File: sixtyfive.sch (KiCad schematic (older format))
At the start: 169 parts, among them J1 Conn_01x12, J2 Conn_ARM_JTAG_SWD_10, Q1 BSS138, SW1 SW_Push, U1 USBLC6-2SC6, U2 STM32F072C8Tx, U3 MCP1700-3302E_SOT23

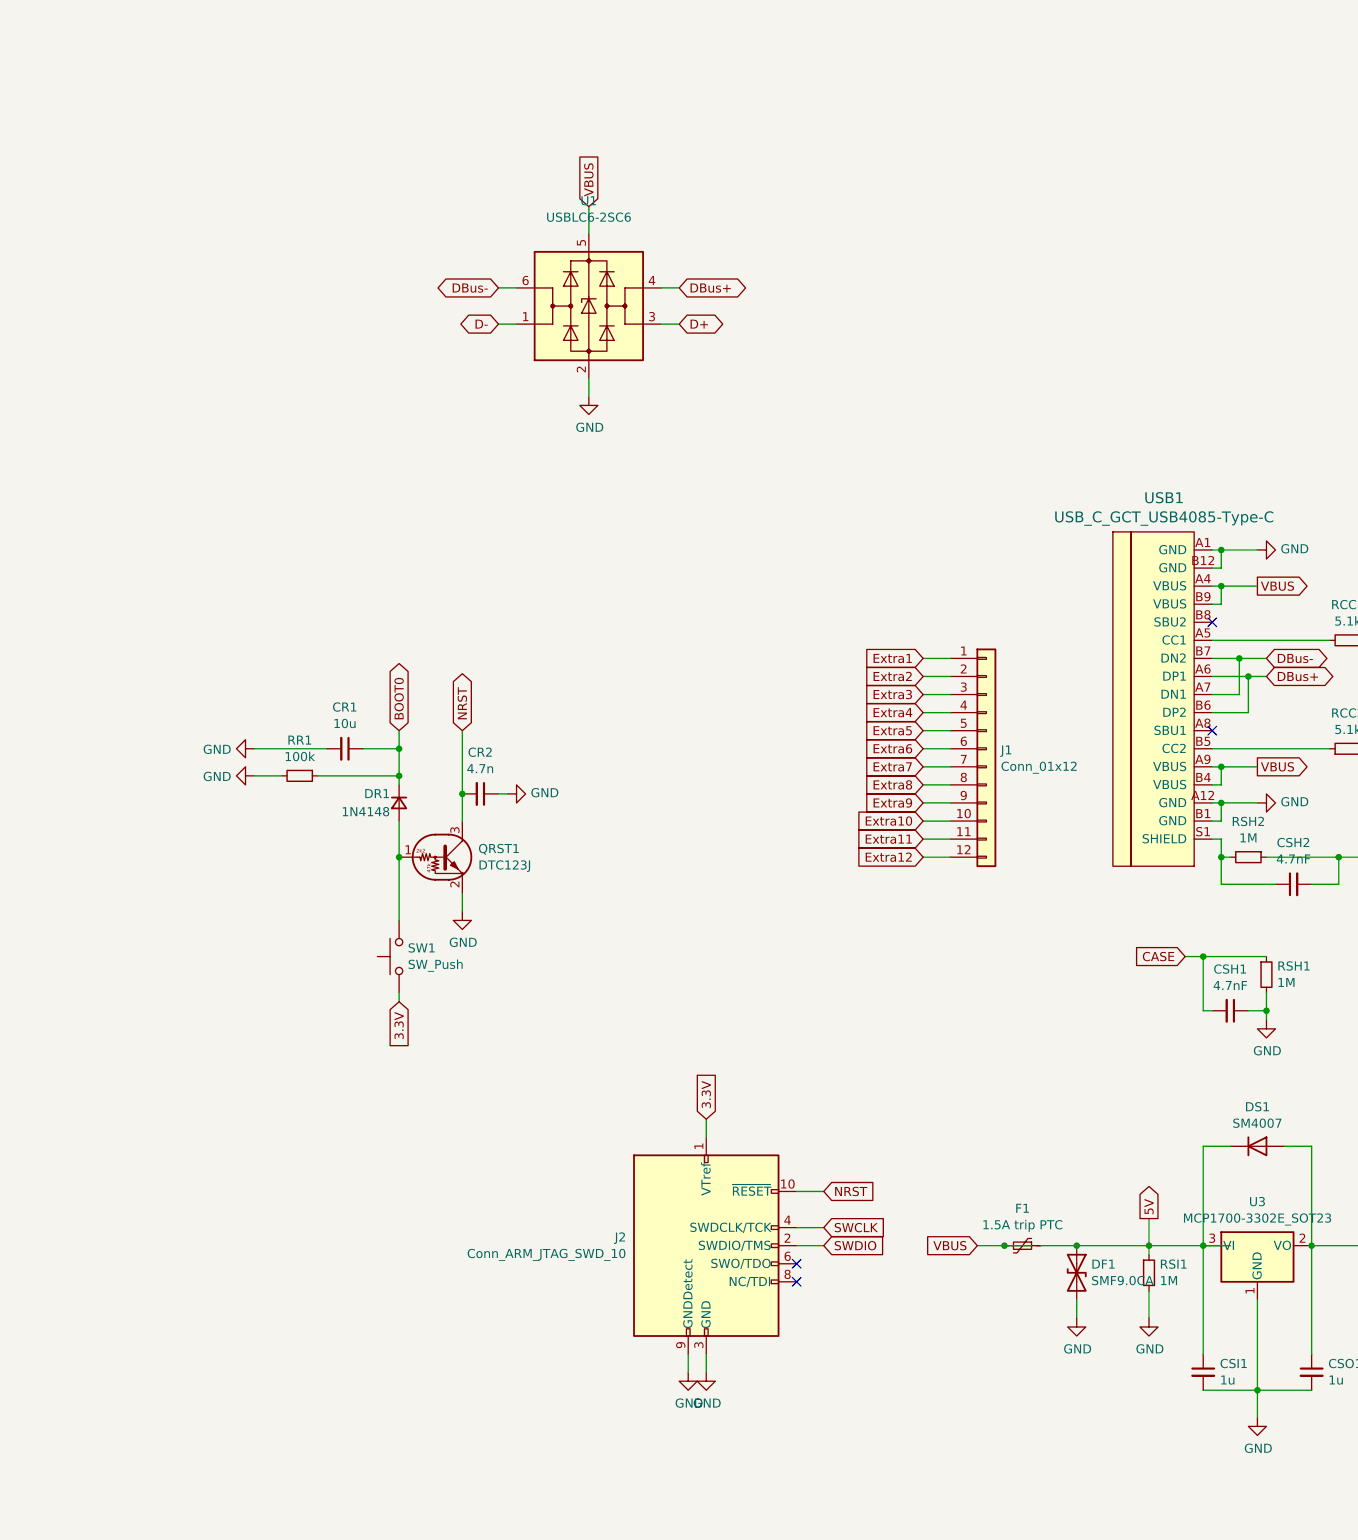
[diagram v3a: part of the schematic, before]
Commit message: swapped a couple components for basic parts, rerouted
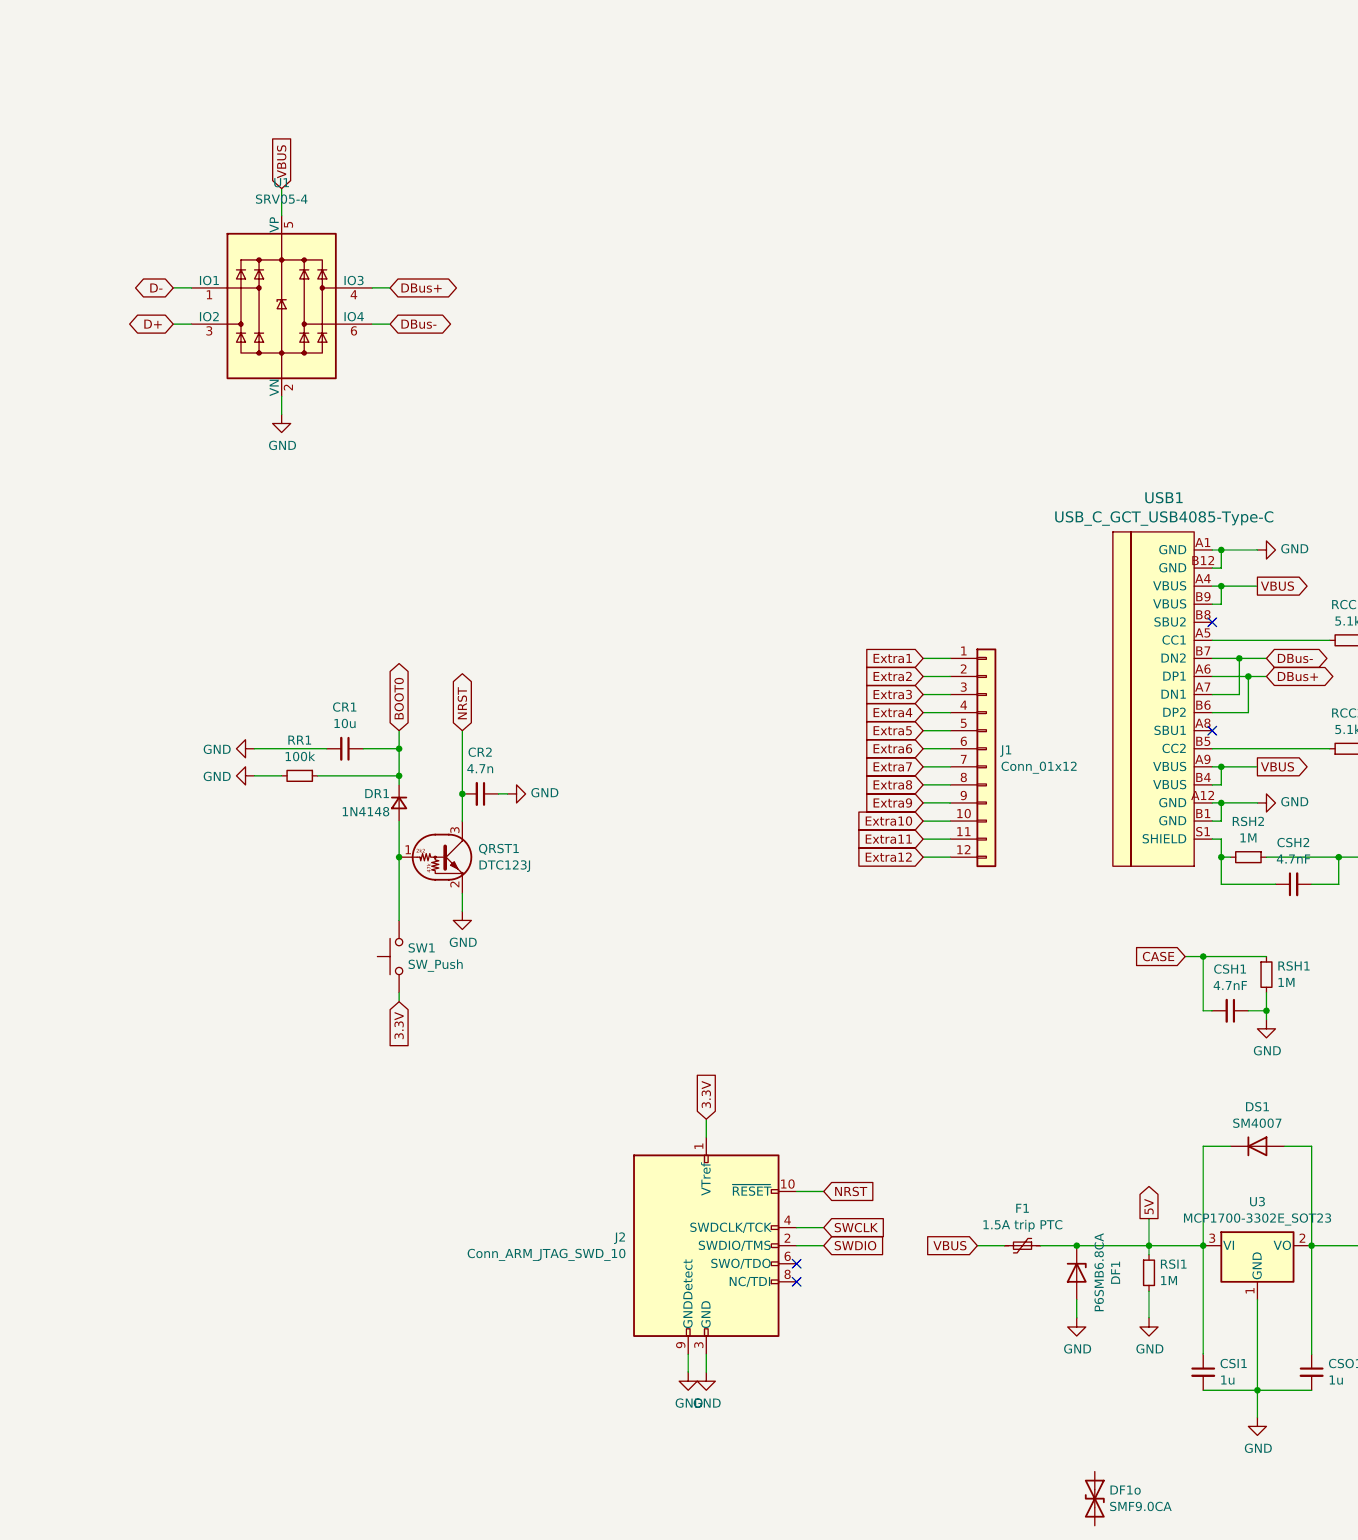
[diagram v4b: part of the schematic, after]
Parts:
- removed U1: USBLC6-2SC6, Package_TO_SOT_SMD:SOT-23-6, symbol Power_Protection:USBLC6-2SC6
- added DF1: P6SMB6.8CA, Diode_SMD:D_SMB, symbol Diode:Z2SMBxxx
- added U1: SRV05-4, Package_TO_SOT_SMD:SOT-23-6, symbol Power_Protection:SRV05-4
- renumbered DF1 to DF1o
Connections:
- net 5V: now also DF1.1 (K); no longer DF1o.1 (A1)
- net D+: now also U1.3 (IO2)
- net D-: now also U1.1 (IO1)
- net DBus+: now also U1.4 (IO3)
- net DBus-: now also U1.6 (IO4)
- net GND: now also DF1.2 (A), U1.2 (VN); no longer DF1o.2 (A2)
- net VBUS: now also U1.5 (VP)
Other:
- moved on the sheet: DF1o
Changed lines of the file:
@@
 $EndComp
 $Comp
-L Device:D_TVS DF1
+L Device:D_TVS DF1o
 U 1 1 5F1046D2
-P 24050 21000
-F 0 "DF1" V 24004 21080 50  0000 L CNN
-F 1 "SMF9.0CA" V 24095 21080 50  0000 L CNN
-F 2 "Diode_SMD:D_SOD-123" H 24050 21000 50  0001 C CNN
-F 3 "~" H 24050 21000 50  0001 C CNN
-F 4 "C123799" V 24050 21000 50  0001 C CNN "JLCCode"
-	1    24050 21000
+P 24150 22250
+F 0 "DF1o" V 24104 22330 50  0000 L CNN
+F 1 "SMF9.0CA" V 24195 22330 50  0000 L CNN
+F 2 "Diode_SMD:D_SOD-123" H 24150 22250 50  0001 C CNN
+F 3 "~" H 24150 22250 50  0001 C CNN
+F 4 "C123799" V 24150 22250 50  0001 C CNN "JLCCode"
+	1    24150 22250
 	0    1    1    0
 $EndComp
 Wire Wire Line
-	23850 20850 24050 20850
-Wire Wire Line
-	24050 20850 24450 20850
-Wire Wire Line
 	24450 20850 24450 20900
-Connection ~ 24050 20850
-$Comp
-L Regulator_Linear:MCP1700-3302E_SOT23 U3
-U 1 1 5F106F9B
-P 25050 20850
-F 0 "U3" H 25050 21092 50  0000 C CNN
-F 1 "MCP1700-3302E_SOT23" H 25050 21001 50  0000 C CNN
-F 2 "Package_TO_SOT_SMD:SOT-23" H 25050 21075 50  0001 C CNN
-F 3 "http://ww1.microchip.com/downloads/en/DeviceDoc/20001826D.pdf" H 25050 20850 50  0001 C CNN
-F 4 "C39051" H 25050 20850 50  0001 C CNN "JLCCode"
-	1    25050 20850
-	1    0    0    -1
-$EndComp
 Connection ~ 24450 20850
 $Comp
@@
 Connection ~ 24850 18400
 Wire Wire Line
-	24750 20850 24900 20850
-Wire Wire Line
 	24450 20850 24750 20850
 Wire Wire Line
@@
 	0    -1   -1   0
 $EndComp
-$Comp
-L Power_Protection:USBLC6-2SC6 U1
-U 1 1 60E168FE
-P 21350 15650
-F 0 "U1" H 21350 16231 50  0000 C CNN
-F 1 "USBLC6-2SC6" H 21350 16140 50  0000 C CNN
-F 2 "Package_TO_SOT_SMD:SOT-23-6" H 21350 15150 50  0001 C CNN
-F 3 "https://www.st.com/resource/en/datasheet/usblc6-2.pdf" H 21550 16000 50  0001 C CNN
-F 4 "C7519" H 21350 15650 50  0001 C CNN "JLCPCB"
-	1    21350 15650
-	1    0    0    -1
-$EndComp
-Text GLabel 21350 15100 1    50   Input ~ 0
+Text GLabel 19650 15000 1    50   Input ~ 0
 VBUS
 Wire Wire Line
-	21350 15100 21350 15250
+	19650 15000 19650 15150
 $Comp
 L power:GND #PWR0141
 U 1 1 60E63053
-P 21350 16150
-F 0 "#PWR0141" H 21350 15900 50  0001 C CNN
-F 1 "GND" H 21355 15977 50  0000 C CNN
-F 2 "" H 21350 16150 50  0001 C CNN
-F 3 "" H 21350 16150 50  0001 C CNN
-	1    21350 16150
+P 19650 16250
+F 0 "#PWR0141" H 19650 16000 50  0001 C CNN
+F 1 "GND" H 19655 16077 50  0000 C CNN
+F 2 "" H 19650 16250 50  0001 C CNN
+F 3 "" H 19650 16250 50  0001 C CNN
+	1    19650 16250
 	1    0    0    -1
 $EndComp
 Wire Wire Line
-	21350 16150 21350 16050
-Text GLabel 21850 15750 2    50   BiDi ~ 0
+	19650 16250 19650 16150
+Text GLabel 19050 15750 0    50   BiDi ~ 0
 D+
-Text GLabel 20850 15750 0    50   BiDi ~ 0
+Text GLabel 19050 15550 0    50   BiDi ~ 0
 D-
-Text GLabel 20850 15550 0    50   BiDi ~ 0
+Text GLabel 20250 15750 2    50   BiDi ~ 0
 DBus-
-Text GLabel 21850 15550 2    50   BiDi ~ 0
+Text GLabel 20250 15550 2    50   BiDi ~ 0
 DBus+
 Wire Wire Line
-	20950 15550 20850 15550
+	20150 15750 20250 15750
 Wire Wire Line
-	20850 15750 20950 15750
+	19050 15550 19150 15550
 Wire Wire Line
-	21750 15750 21850 15750
+	19150 15750 19050 15750
 Wire Wire Line
-	21850 15550 21750 15550
+	20250 15550 20150 15550
 $Comp
 L power:GNDD #PWR0142
@@
 Wire Wire Line
 	23650 20850 23500 20850
-Connection ~ 23650 20850
-Wire Wire Line
-	23650 20850 23800 20850
 $Comp
 L Diode:BAV70 D1
@@
 Wire Wire Line
 	25350 20850 25800 20850
+$Comp
+L Power_Protection:SRV05-4 U1
+U 1 1 5EEE073D
+P 19650 15650
+F 0 "U1" H 19650 16331 50  0000 C CNN
+F 1 "SRV05-4" H 19650 16240 50  0000 C CNN
+F 2 "Package_TO_SOT_SMD:SOT-23-6" H 20350 15200 50  0001 C CNN
+F 3 "http://www.onsemi.com/pub/Collateral/SRV05-4-D.PDF" H 19650 15650 50  0001 C CNN
+F 4 "C85364" H 19650 15650 50  0001 C CNN "JLCCode"
+	1    19650 15650
+	1    0    0    -1
+$EndComp
+$Comp
+L Regulator_Linear:MCP1700-3302E_SOT23 U3
+U 1 1 5F106F9B
+P 25050 20850
+F 0 "U3" H 25050 21092 50  0000 C CNN
+F 1 "MCP1700-3302E_SOT23" H 25050 21001 50  0000 C CNN
+F 2 "Package_TO_SOT_SMD:SOT-23" H 25050 21075 50  0001 C CNN
+F 3 "http://ww1.microchip.com/downloads/en/DeviceDoc/20001826D.pdf" H 25050 20850 50  0001 C CNN
+F 4 "C39051" H 25050 20850 50  0001 C CNN "JLCCode"
+	1    25050 20850
+	1    0    0    -1
+$EndComp
+$Comp
+L Diode:Z2SMBxxx DF1
+U 1 1 5F28F23A
+P 24050 21000
+F 0 "DF1" H 24050 21217 50  0000 C CNN
+F 1 "P6SMB6.8CA" H 24050 21126 50  0000 C CNN
+F 2 "Diode_SMD:D_SMB" H 24050 20825 50  0001 C CNN
+F 3 "https://datasheet.lcsc.com/szlcsc/Brightking-Elec-TAIWAN-P6SMB6-8CA_C78395.pdf" H 24050 21000 50  0001 C CNN
+F 4 "C78395" H 24050 21000 50  0001 C CNN "JLCCode"
+	1    24050 21000
+	0    1    1    0
+$EndComp
+Wire Wire Line
+	23850 20850 24050 20850
+Connection ~ 24050 20850
+Wire Wire Line
+	24050 20850 24450 20850
 $EndSCHEMATC

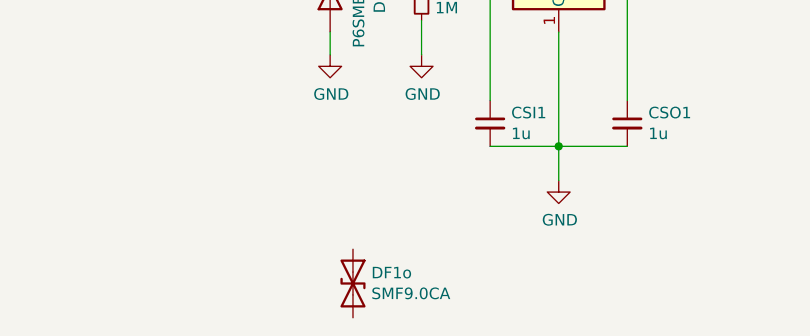
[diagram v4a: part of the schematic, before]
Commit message: Didn't quite save everything that last time.
Just following the last bit of advice from the discord, swapping a couple components and rerouting some things
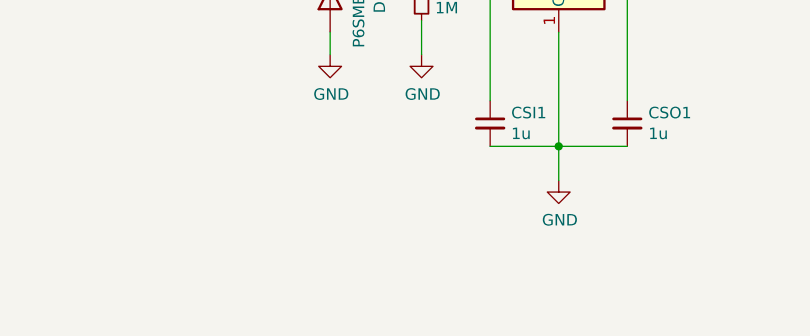
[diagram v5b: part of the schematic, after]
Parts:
- removed DF1o: SMF9.0CA, Diode_SMD:D_SOD-123, symbol Device:D_TVS
- DF1: footprint Diode_SMD:D_SMB -> Diode_SMD:D_SOD-123
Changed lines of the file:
@@
 	1    0    0    -1
 $EndComp
-$Comp
-L Device:D_TVS DF1o
-U 1 1 5F1046D2
-P 24150 22250
-F 0 "DF1o" V 24104 22330 50  0000 L CNN
-F 1 "SMF9.0CA" V 24195 22330 50  0000 L CNN
-F 2 "Diode_SMD:D_SOD-123" H 24150 22250 50  0001 C CNN
-F 3 "~" H 24150 22250 50  0001 C CNN
-F 4 "C123799" V 24150 22250 50  0001 C CNN "JLCCode"
-	1    24150 22250
-	0    1    1    0
-$EndComp
 Wire Wire Line
 	24450 20850 24450 20900
@@
 F 0 "DF1" H 24050 21217 50  0000 C CNN
 F 1 "P6SMB6.8CA" H 24050 21126 50  0000 C CNN
-F 2 "Diode_SMD:D_SMB" H 24050 20825 50  0001 C CNN
+F 2 "Diode_SMD:D_SOD-123" H 24050 20825 50  0001 C CNN
 F 3 "https://datasheet.lcsc.com/szlcsc/Brightking-Elec-TAIWAN-P6SMB6-8CA_C78395.pdf" H 24050 21000 50  0001 C CNN
 F 4 "C78395" H 24050 21000 50  0001 C CNN "JLCCode"

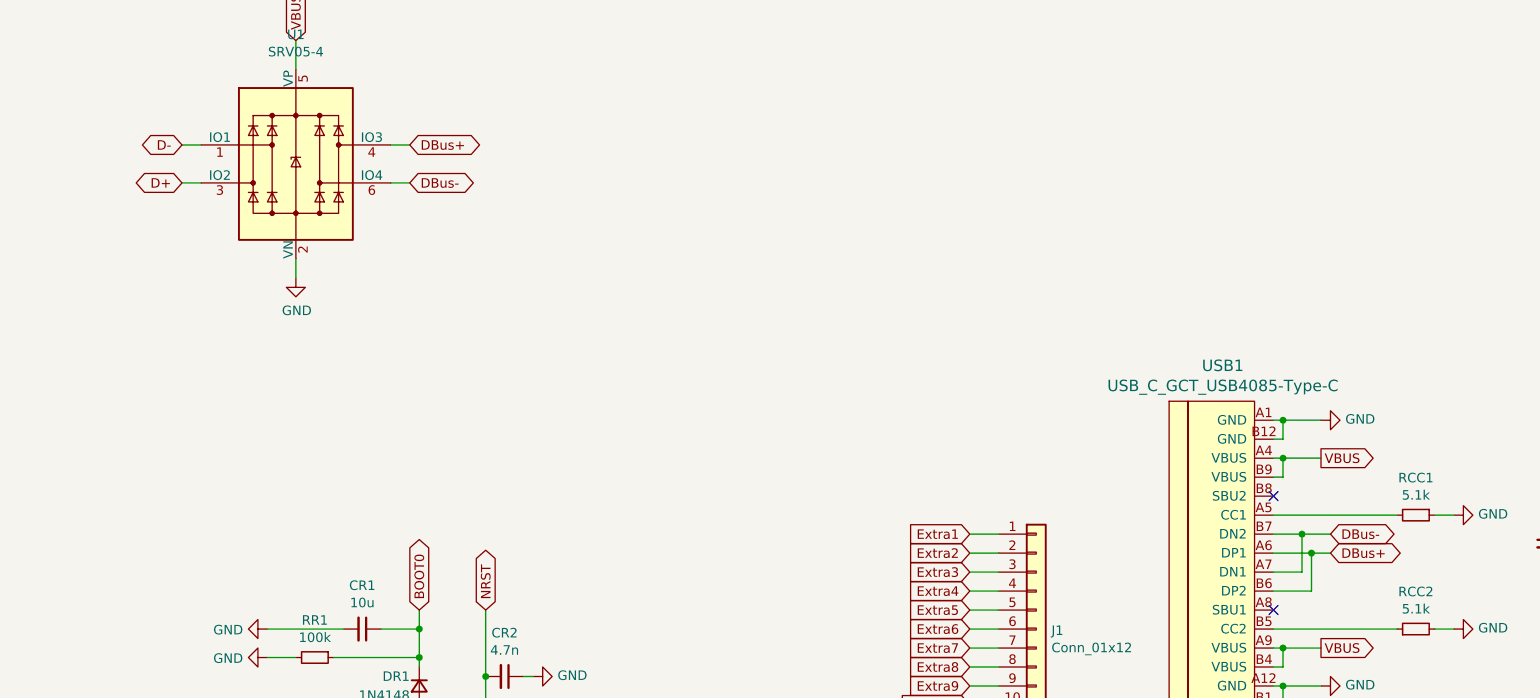
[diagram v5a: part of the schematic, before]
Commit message: Further discord feedback, using the srv05 properly now
using the component right this time
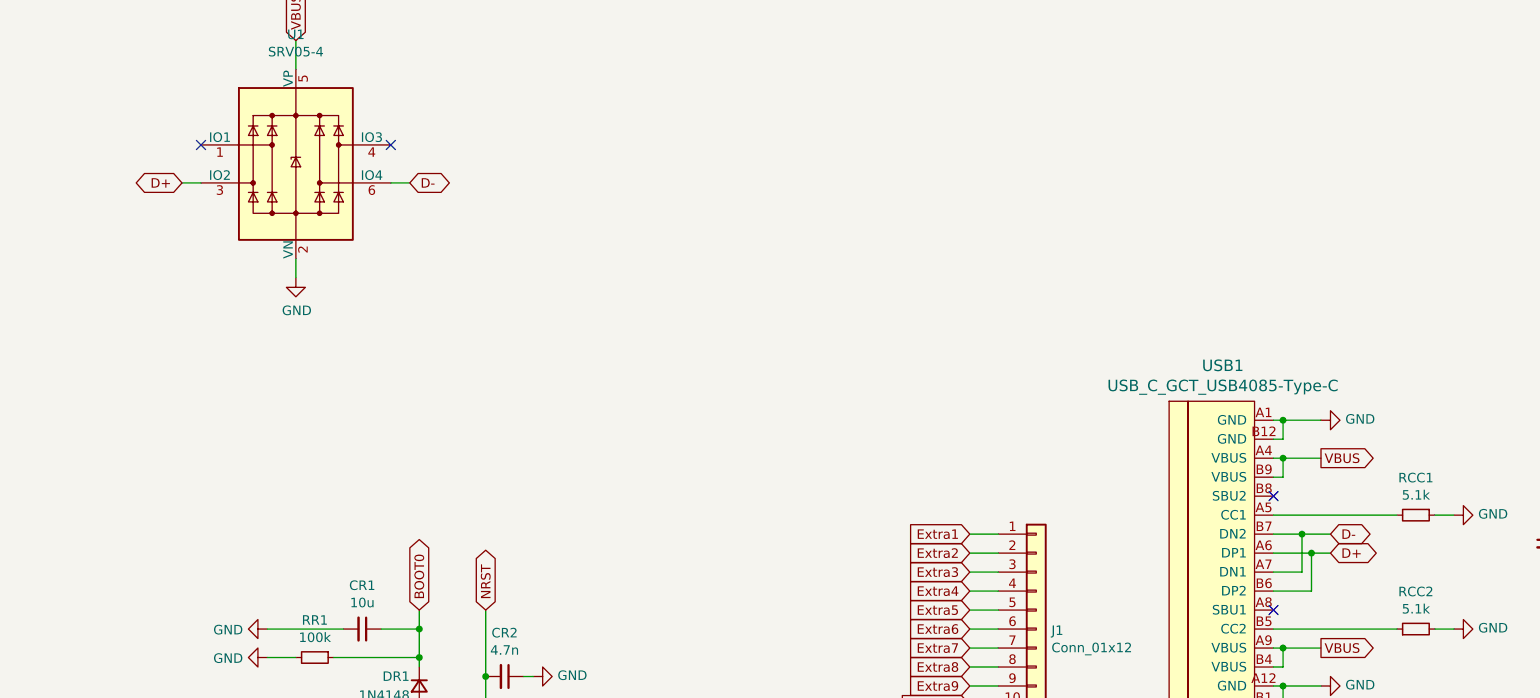
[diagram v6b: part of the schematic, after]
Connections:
- net DBus- is gone; now on net D-: U1.6 (IO4), USB1.A7 (DN1), USB1.B7 (DN2)
- net D+: now also USB1.A6 (DP1), USB1.B6 (DP2)
- net D-: no longer U1.1 (IO1)
- removed net DBus+: U1.4 (IO3), USB1.A6 (DP1), USB1.B6 (DP2)
- no-connect marks 4 -> 6
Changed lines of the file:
@@
 NoConn ~ 24800 17400
 Text GLabel 25100 17700 2    50   BiDi ~ 0
-DBus+
+D+
 Text GLabel 25100 17600 2    50   BiDi ~ 0
-DBus-
+D-
 Wire Wire Line
 	24800 17600 24950 17600
@@
 Text GLabel 19050 15750 0    50   BiDi ~ 0
 D+
-Text GLabel 19050 15550 0    50   BiDi ~ 0
-D-
 Text GLabel 20250 15750 2    50   BiDi ~ 0
-DBus-
-Text GLabel 20250 15550 2    50   BiDi ~ 0
-DBus+
+D-
 Wire Wire Line
 	20150 15750 20250 15750
 Wire Wire Line
-	19050 15550 19150 15550
-Wire Wire Line
 	19150 15750 19050 15750
-Wire Wire Line
-	20250 15550 20150 15550
 $Comp
 L power:GNDD #PWR0142
@@
 Wire Wire Line
 	24050 20850 24450 20850
+NoConn ~ 20150 15550
+NoConn ~ 19150 15550
 $EndSCHEMATC
